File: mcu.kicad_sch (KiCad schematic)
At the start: 14 parts, among them J2 Conn_01x05_Pin, J3 Conn_01x10_Pin, SW1 TS-1088R-02026, SW2 TS-1088R-02026, U2 ESP-12F

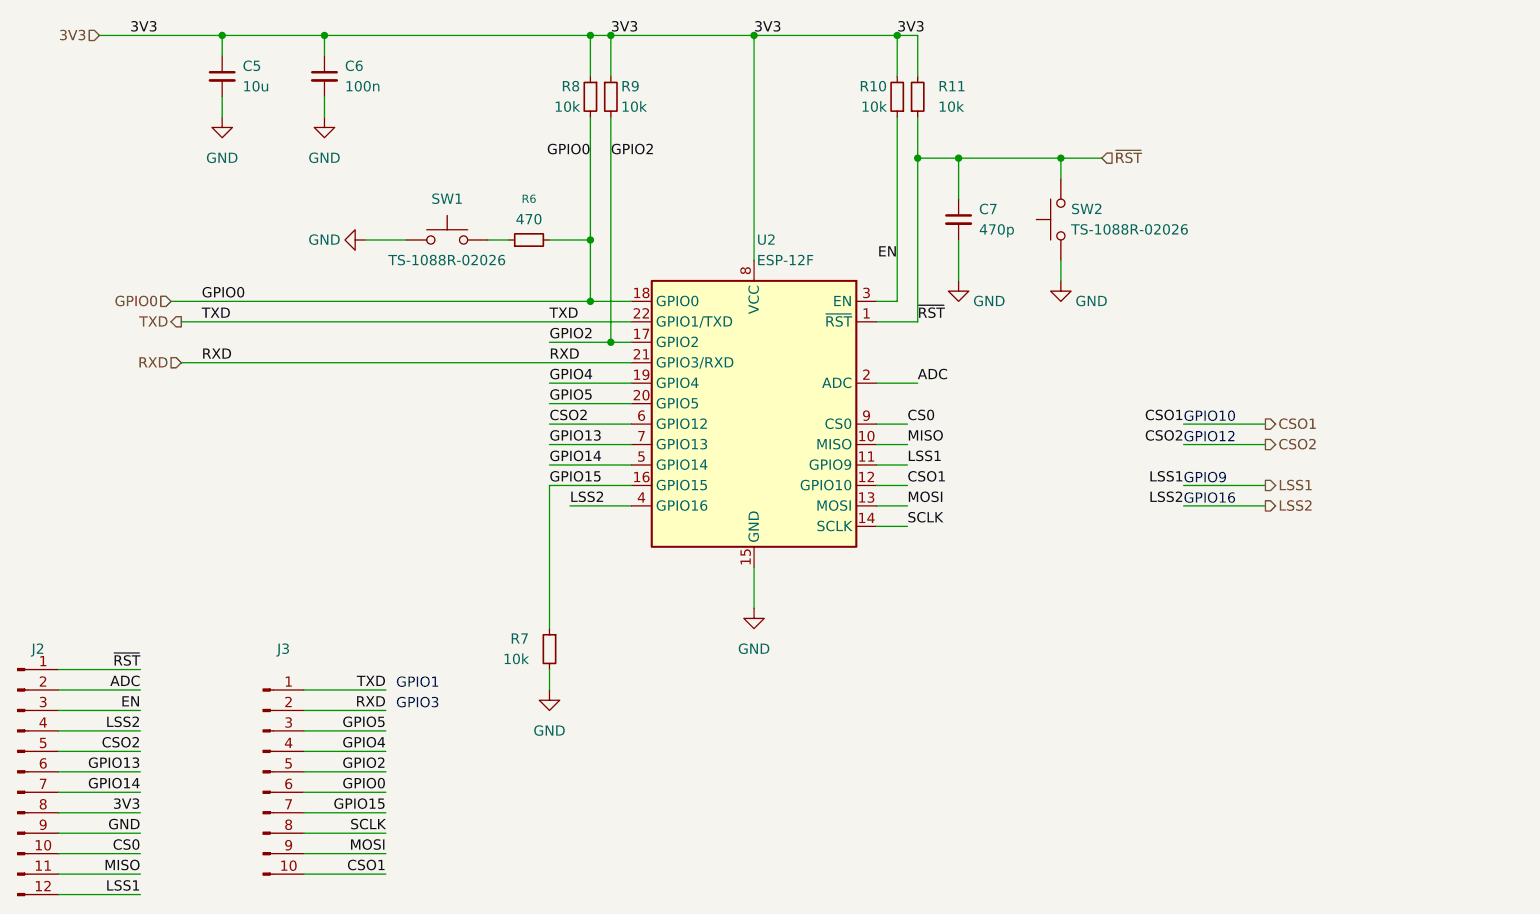
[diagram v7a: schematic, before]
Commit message: Correct unusable FLASH SPI pins
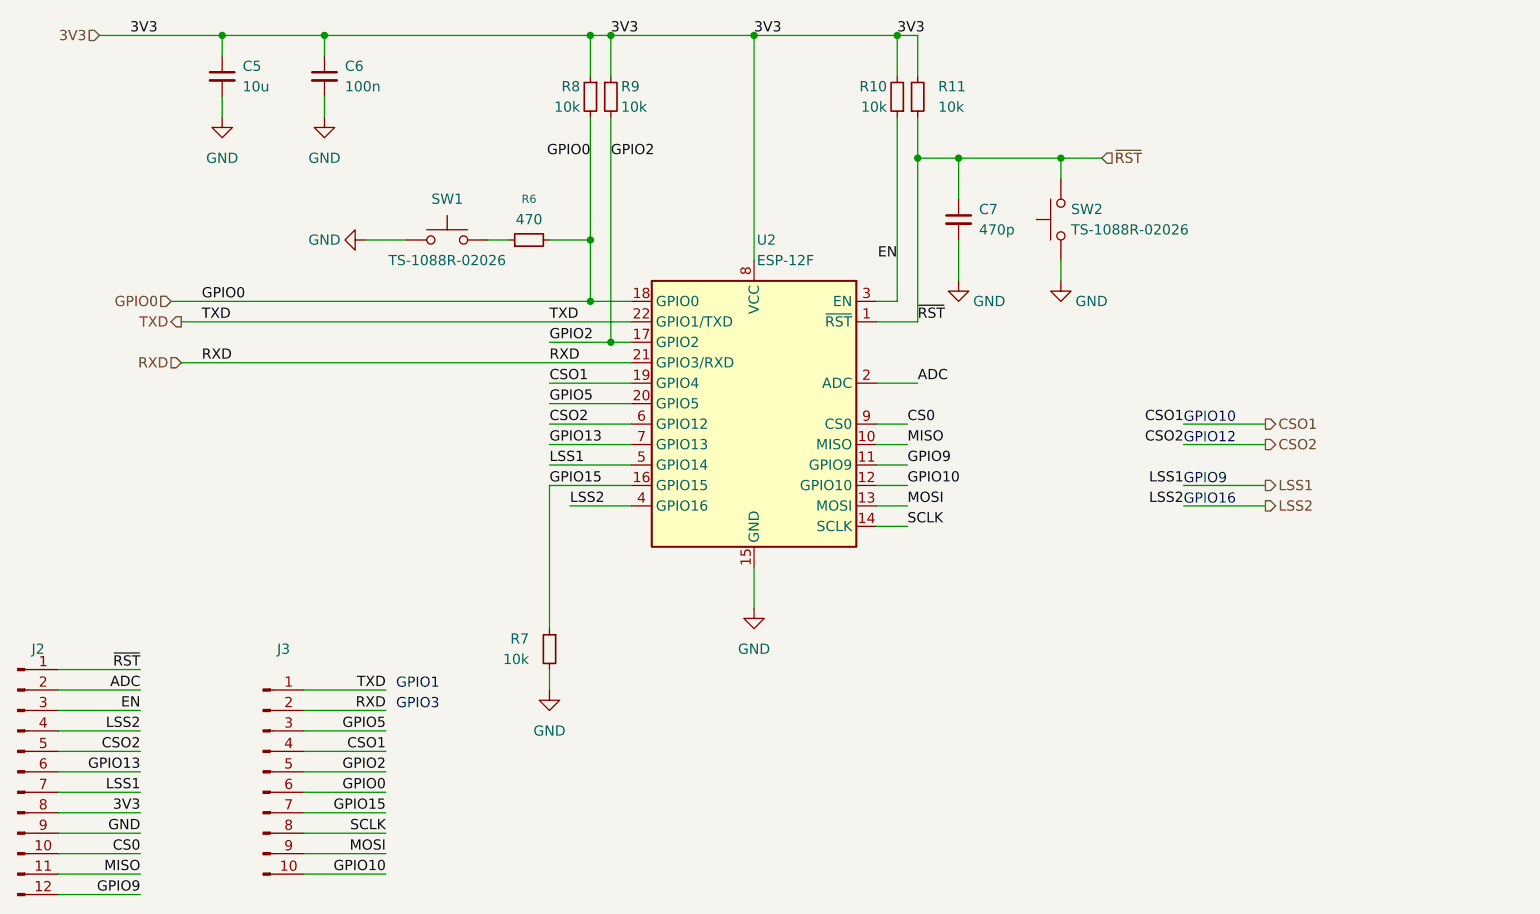
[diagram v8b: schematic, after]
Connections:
- net GPIO14 is gone; now on net LSS1: J2.7 (Pin_7), U2.5 (GPIO14)
- net GPIO4 is gone; now on net CSO1: J3.4 (Pin_4), U2.19 (GPIO4)
- net CSO1: no longer J3.10 (Pin_10), U2.12 (GPIO10)
- net LSS1: no longer J2.12 (Pin_12), U2.11 (GPIO9)
- new net GPIO10: J3.10 (Pin_10), U2.12 (GPIO10)
- new net GPIO9: J2.12 (Pin_12), U2.11 (GPIO9)
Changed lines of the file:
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@@
+		)
+	)
+	(label "GPIO9"
+		(at 83.82 162.56 180)
+		(effects
+			(font
+				(size 1.27 1.27)
+			)
+			(justify right bottom)
+		)
+	)
+	(label "GPIO10"
+		(at 179.07 111.76 0)
+		(effects
+			(font
+				(size 1.27 1.27)
+			)
+			(justify left bottom)
 		)
 	)
@@
 		)
 	)
-	(label "CSO1"
-		(at 114.3 160.02 180)
-		(effects
-			(font
-				(size 1.27 1.27)
-			)
-			(justify right bottom)
-		)
-	)
 	(label "~{RST}"
 		(at 83.82 134.62 180)
@@
 		)
 	)
-	(label "CSO1"
-		(at 179.07 111.76 0)
-		(effects
-			(font
-				(size 1.27 1.27)
-			)
-			(justify left bottom)
-		)
-	)
 	(label "~{RST}"
 		(at 180.34 91.44 0)
@@
 		)
 	)
+	(label "CSO1"
+		(at 134.62 99.06 0)
+		(effects
+			(font
+				(size 1.27 1.27)
+			)
+			(justify left bottom)
+		)
+	)
 	(label "3V3"
 		(at 82.55 55.88 0)
@@
 		)
 	)
+	(label "LSS1"
+		(at 134.62 109.22 0)
+		(effects
+			(font
+				(size 1.27 1.27)
+			)
+			(justify left bottom)
+		)
+	)
+	(label "GPIO10"
+		(at 114.3 160.02 180)
+		(effects
+			(font
+				(size 1.27 1.27)
+			)
+			(justify right bottom)
+		)
+	)
 	(label "LSS2"
 		(at 83.82 142.24 180)
@@
 		)
 	)
+	(label "LSS1"
+		(at 83.82 149.86 180)
+		(effects
+			(font
+				(size 1.27 1.27)
+			)
+			(justify right bottom)
+		)
+	)
 	(label "CS0"
 		(at 179.07 104.14 0)
@@
 		)
 	)
-	(label "GPIO4"
+	(label "CSO1"
 		(at 114.3 144.78 180)
 		(effects
@@
 		)
 	)
-	(label "LSS1"
-		(at 83.82 162.56 180)
-		(effects
-			(font
-				(size 1.27 1.27)
-			)
-			(justify right bottom)
+	(label "GPIO9"
+		(at 179.07 109.22 0)
+		(effects
+			(font
+				(size 1.27 1.27)
+			)
+			(justify left bottom)
 		)
 	)
@@
 		)
 	)
-	(label "GPIO4"
-		(at 134.62 99.06 0)
-		(effects
-			(font
-				(size 1.27 1.27)
-			)
-			(justify left bottom)
-		)
-	)
 	(label "GPIO5"
 		(at 114.3 142.24 180)
@@
 		)
 	)
-	(label "GPIO14"
-		(at 134.62 109.22 0)
-		(effects
-			(font
-				(size 1.27 1.27)
-			)
-			(justify left bottom)
-		)
-	)
-	(label "GPIO14"
-		(at 83.82 149.86 180)
-		(effects
-			(font
-				(size 1.27 1.27)
-			)
-			(justify right bottom)
-		)
-	)
-	(label "LSS1"
-		(at 179.07 109.22 0)
-		(effects
-			(font
-				(size 1.27 1.27)
-			)
-			(justify left bottom)
-		)
-	)
